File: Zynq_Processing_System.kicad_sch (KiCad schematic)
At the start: 51 parts, among them Q100 T2N7002AK,LM, SW300 SKRPANE010, U200 XC7Z010-2CLG400I, U400 74LVC1G07, U401 74LVC1G07, U402 W25Q128JVEIQ, U403 S40FC004C1B2C00000, X400 ECS-2520MV-333.3-BN-TR

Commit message: Added page '[7] 1GB DDR3L Modules'
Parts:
- renumbered C101 to C400, C101 to C401, C101 to C402, C120 to C403, C120 to C404, C101 to C405, C101 to C406, C101 to C407, C126 to C408, C101 to C409, C126 to C410, C126 to C411, C101 to C412, C126 to C413, D101 to D400, Q100 to Q400, R103 to R400, R103 to R401, R103 to R402, R102 to R403, R127 to R404, R127 to R405, R102 to R406, R102 to R407, R102 to R408, R102 to R409, R102 to R410, R102 to R411, R123 to R412, R103 to R413, R104 to R414, R104 to R416, R103 to R417, R103 to R418, R102 to R419, R102 to R420, R106 to R421, R106 to R422, R106 to R423, R106 to R424, R103 to R425, R103 to R426, R102 to R427, R127 to R428, SW300 to SW400
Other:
- company: (none) -> Designed By: Dylan Gutierrez

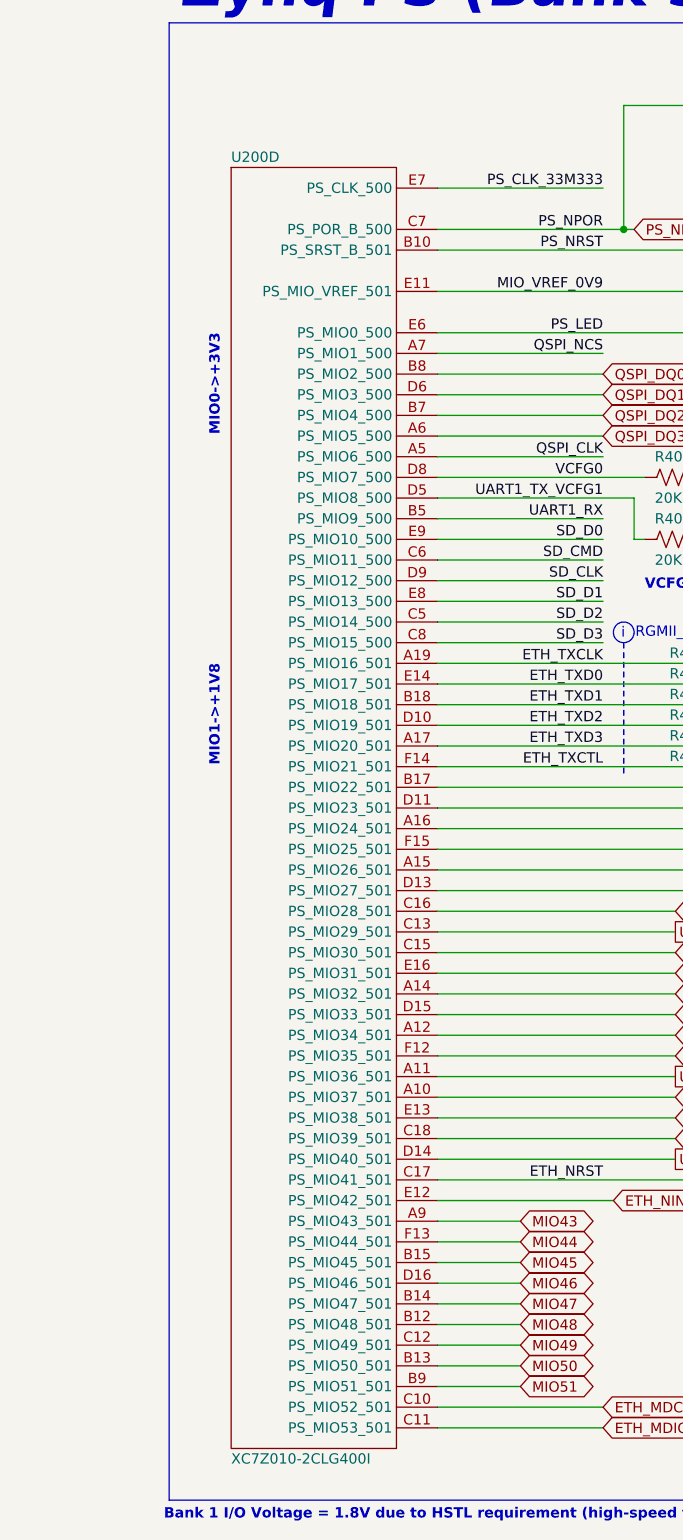
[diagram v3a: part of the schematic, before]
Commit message: Finished first pass of schematic, needs netclass assignments and double check
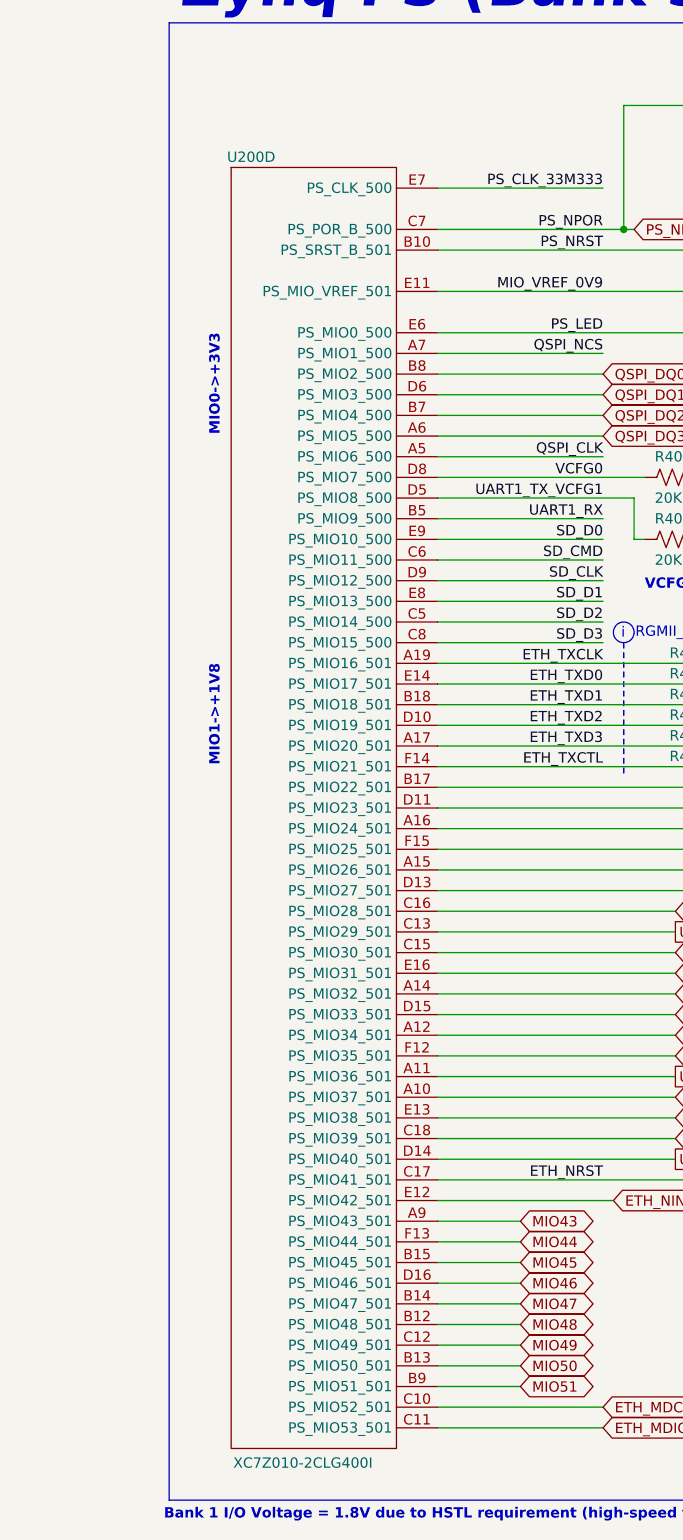
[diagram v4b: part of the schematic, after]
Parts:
- U402: footprint Package_SON:WSON-8-1EP_8x6mm_P1.27mm_EP3.4x4.3mm -> ZeBra_footprints:WSON-8-1EP_8x6mm_P1.27mm_EP3.4x4.3mm
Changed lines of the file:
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@@
 		(dnp no)
 		(property "Reference" "U200"
-			(at 25.4 73.66 0)
+			(at 24.892 73.66 0)
 			(effects
 				(font
@@
 		)
 		(property "Value" "XC7Z010-2CLG400I"
-			(at 25.4 233.68 0)
+			(at 25.654 234.188 0)
 			(effects
 				(font
@@
 					(unit 4)
 				)
+				(path "/ec71d28a-654e-4dfb-b412-dd09b7b3e4b8/369d50d7-e508-4bcb-a2d0-a2c7d0c5b870"
+					(reference "U200")
+					(unit 4)
+				)
 			)
 		)
@@
 			)
 		)
-		(property "Footprint" "Package_SON:WSON-8-1EP_8x6mm_P1.27mm_EP3.4x4.3mm"
+		(property "Footprint" "ZeBra_footprints:WSON-8-1EP_8x6mm_P1.27mm_EP3.4x4.3mm"
 			(at 280.67 83.82 0)
 			(effects
